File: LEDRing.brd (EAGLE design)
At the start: 52.5 x 52.4 mm, 35 parts, among them U1 ATMEGA328P-AU, U2 MCP73831, U3 MIC5219 3.3V, U4 MMA8452Q, Y1 16MHZ

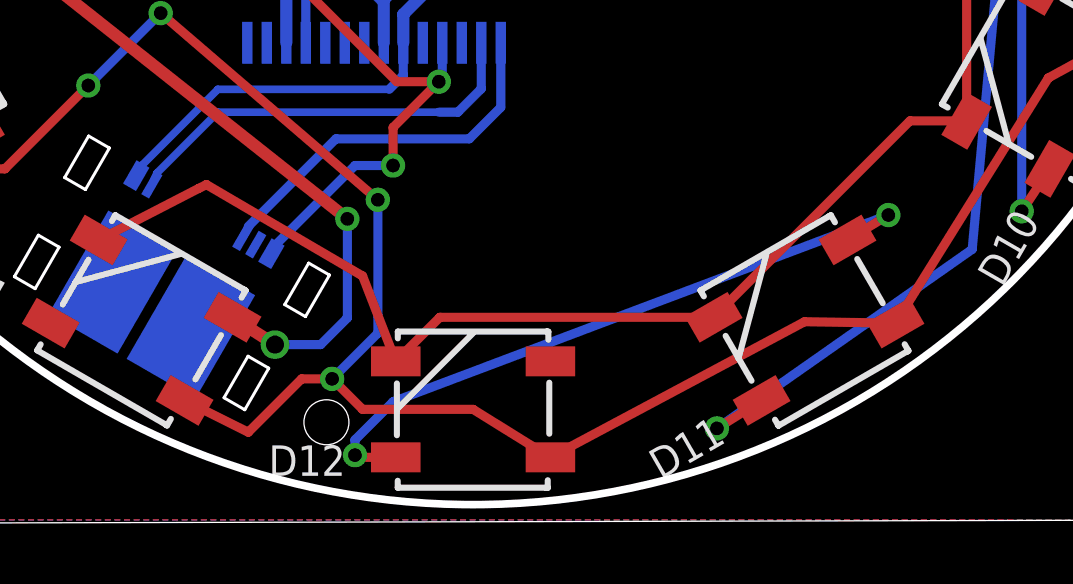
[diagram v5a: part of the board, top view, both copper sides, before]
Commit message: Removed most USB footprint errors
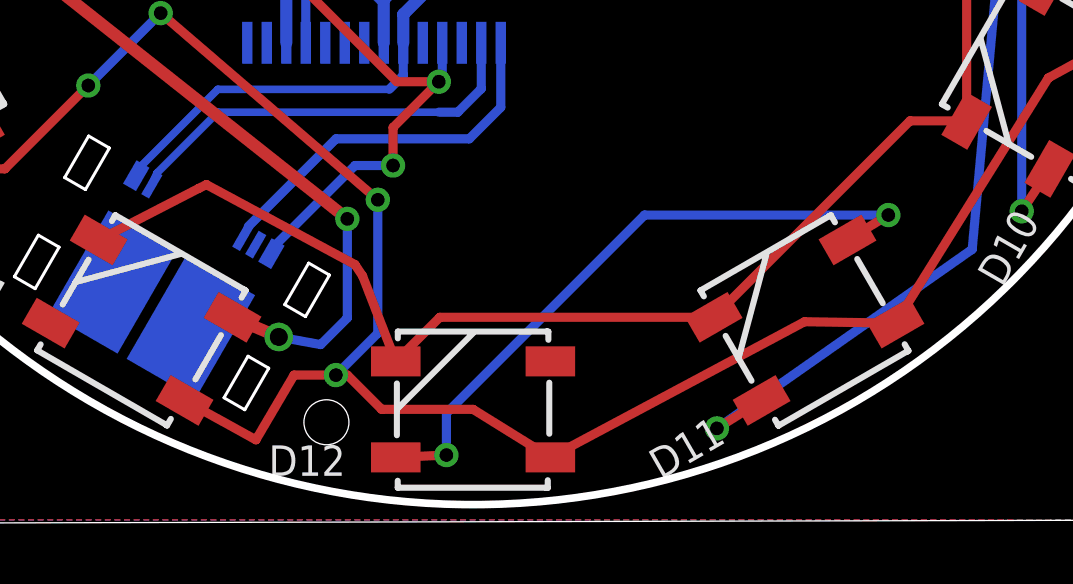
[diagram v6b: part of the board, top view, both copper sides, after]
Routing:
- net N$24: track 22.9 -> 22.1 mm
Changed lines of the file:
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@@
 <wire x1="23.495" y1="11.938" x2="23.495" y2="13.208" width="0.3048" layer="1"/>
 <wire x1="23.495" y1="13.208" x2="25.019" y2="14.732" width="0.3048" layer="1"/>
-<wire x1="29.171" y1="37.592" x2="31.50611875" y2="39.543221875" width="0" layer="19" extent="1-1"/>
-<wire x1="28.956" y1="37.084" x2="29.171" y2="37.592" width="0" layer="19" extent="1-16"/>
-<wire x1="24.887" y1="26.535" x2="26.162" y2="27.31" width="0" layer="19" extent="1-1"/>
-<wire x1="35.5901" y1="27.051" x2="33.655" y2="27.012" width="0" layer="19" extent="1-16"/>
-<wire x1="18.2372" y1="36.2712" x2="26.4668" y2="37.0586" width="0" layer="19" extent="16-16"/>
-<wire x1="18.2372" y1="37.8714" x2="18.2372" y2="36.2712" width="0" layer="19" extent="16-16"/>
-<wire x1="15.748" y1="39.878" x2="18.2372" y2="37.8714" width="0" layer="19" extent="16-16"/>
 </signal>
 <signal name="N$1">
@@
 <wire x1="44.45" y1="31.877" x2="48.26" y2="31.877" width="0.3048" layer="16"/>
 <wire x1="48.26" y1="31.877" x2="49.911" y2="30.226" width="0.3048" layer="16"/>
-<wire x1="26.162" y1="3.81" x2="22.479" y2="3.81" width="0.3048" layer="1"/>
-<wire x1="22.479" y1="3.81" x2="21.463" y2="4.826" width="0.3048" layer="1"/>
-<wire x1="20.447" y1="4.826" x2="18.669" y2="3.048" width="0.3048" layer="1"/>
-<wire x1="18.669" y1="3.048" x2="16.544746875" y2="4.10765625" width="0.3048" layer="1"/>
+<wire x1="20.193" y1="4.953" x2="18.923" y2="2.794" width="0.3048" layer="1"/>
+<wire x1="18.923" y1="2.794" x2="16.544746875" y2="4.10765625" width="0.3048" layer="1"/>
 <wire x1="6.93865625" y1="11.82725" x2="10.55725" y2="11.82725" width="0.3048" layer="1"/>
 <wire x1="10.55725" y1="11.82725" x2="13.335" y2="14.605" width="0.3048" layer="1"/>
@@
 <via x="15.748" y="17.018" extent="1-16" drill="0.4572" diameter="0.254" shape="octagon"/>
 <wire x1="15.748" y1="17.018" x2="22.987" y2="10.795" width="0.3048" layer="1"/>
-<wire x1="20.447" y1="4.826" x2="21.463" y2="4.826" width="0.3048" layer="1"/>
-<via x="21.463" y="4.826" extent="1-16" drill="0.4572" diameter="0.254" shape="octagon"/>
+<wire x1="20.193" y1="4.953" x2="21.59" y2="4.953" width="0.3048" layer="1"/>
+<via x="21.59" y="4.953" extent="1-16" drill="0.4572" diameter="0.254" shape="octagon"/>
 <via x="22.987" y="10.795" extent="1-16" drill="0.4572" diameter="0.254" shape="octagon"/>
 <wire x1="22.987" y1="10.795" x2="22.987" y2="6.35" width="0.3048" layer="16"/>
-<wire x1="22.987" y1="6.35" x2="21.463" y2="4.826" width="0.3048" layer="16"/>
+<wire x1="22.987" y1="6.35" x2="21.59" y2="4.953" width="0.3048" layer="16"/>
+<wire x1="21.59" y1="4.953" x2="21.971" y2="4.953" width="0.3048" layer="1"/>
+<wire x1="21.971" y1="4.953" x2="23.114" y2="3.81" width="0.3048" layer="1"/>
+<wire x1="23.114" y1="3.81" x2="26.162" y2="3.81" width="0.3048" layer="1"/>
 </signal>
 <signal name="V3_3">
@@
 <wire x1="7.132940625" y1="27.016059375" x2="5.664" y2="28.485" width="0.3048" layer="1"/>
 <wire x1="23.585" y1="5.41" x2="22.479" y2="8.255" width="0.3048" layer="1"/>
-<wire x1="22.479" y1="8.255" x2="17.272" y2="11.303" width="0.3048" layer="1"/>
 <wire x1="17.272" y1="11.303" x2="17.018" y2="11.176" width="0.3048" layer="1"/>
 <wire x1="17.018" y1="11.176" x2="13.68125" y2="9.455940625" width="0.3048" layer="1"/>
@@
 <wire x1="33.782" y1="43.307" x2="31.838" y2="43.307" width="0.4064" layer="1"/>
 <wire x1="31.838" y1="43.307" x2="28.739" y2="46.406" width="0.4064" layer="1"/>
+<wire x1="22.479" y1="8.255" x2="22.225" y2="8.636" width="0.3048" layer="1"/>
+<wire x1="22.225" y1="8.636" x2="17.272" y2="11.303" width="0.3048" layer="1"/>
 </signal>
 <signal name="N$10">
@@
 <wire x1="4.36165625" y1="16.290746875" x2="3.556" y2="17.653" width="0.3048" layer="1"/>
 <via x="3.556" y="17.653" extent="1-16" drill="0.4572" diameter="0.254" shape="octagon"/>
-<wire x1="18.144746875" y1="6.878940625" x2="19.558" y2="5.969" width="0.4064" layer="1"/>
-<via x="19.558" y="5.969" extent="1-16" drill="0.6" shape="octagon"/>
+<wire x1="18.144746875" y1="6.878940625" x2="19.685" y2="6.223" width="0.4064" layer="1"/>
+<via x="19.685" y="6.223" extent="1-16" drill="0.6" shape="octagon"/>
 <via x="21.971" y="10.16" extent="1-16" drill="0.4572" diameter="0.254" shape="octagon"/>
 <wire x1="21.971" y1="10.16" x2="8.509" y2="20.828" width="0.4064" layer="1"/>
@@
 <wire x1="21.971" y1="10.16" x2="21.971" y2="6.858" width="0.3048" layer="16"/>
 <wire x1="21.971" y1="6.858" x2="21.082" y2="5.969" width="0.3048" layer="16"/>
-<wire x1="21.082" y1="5.969" x2="19.558" y2="5.969" width="0.3048" layer="16"/>
+<wire x1="21.082" y1="5.969" x2="19.685" y2="6.223" width="0.3048" layer="16"/>
 </signal>
 <signal name="N$16">
@@
 <via x="40.005" y="10.287" extent="1-16" drill="0.4572" diameter="0.254" shape="octagon"/>
 <wire x1="38.642746875" y1="9.455940625" x2="40.005" y2="10.287" width="0.3048" layer="1"/>
-<wire x1="23.585" y1="2.21" x2="22.301" y2="2.21" width="0.3048" layer="1"/>
-<wire x1="22.301" y1="2.21" x2="22.225" y2="2.286" width="0.3048" layer="1"/>
-<via x="22.225" y="2.286" extent="1-16" drill="0.4572" diameter="0.254" shape="octagon"/>
-<wire x1="22.225" y1="2.286" x2="22.225" y2="2.794" width="0.3048" layer="16"/>
-<wire x1="22.225" y1="2.794" x2="23.495" y2="4.064" width="0.3048" layer="16"/>
-<wire x1="23.495" y1="4.064" x2="40.005" y2="10.287" width="0.3048" layer="16"/>
+<via x="25.273" y="2.286" extent="1-16" drill="0.4572" diameter="0.254" shape="octagon"/>
+<wire x1="23.585" y1="2.21" x2="25.273" y2="2.286" width="0.3048" layer="1"/>
+<wire x1="40.005" y1="10.287" x2="31.877" y2="10.287" width="0.3048" layer="16"/>
+<wire x1="31.877" y1="10.287" x2="25.273" y2="3.683" width="0.3048" layer="16"/>
+<wire x1="25.273" y1="3.683" x2="25.273" y2="2.286" width="0.3048" layer="16"/>
 </signal>
 <signal name="N$14">

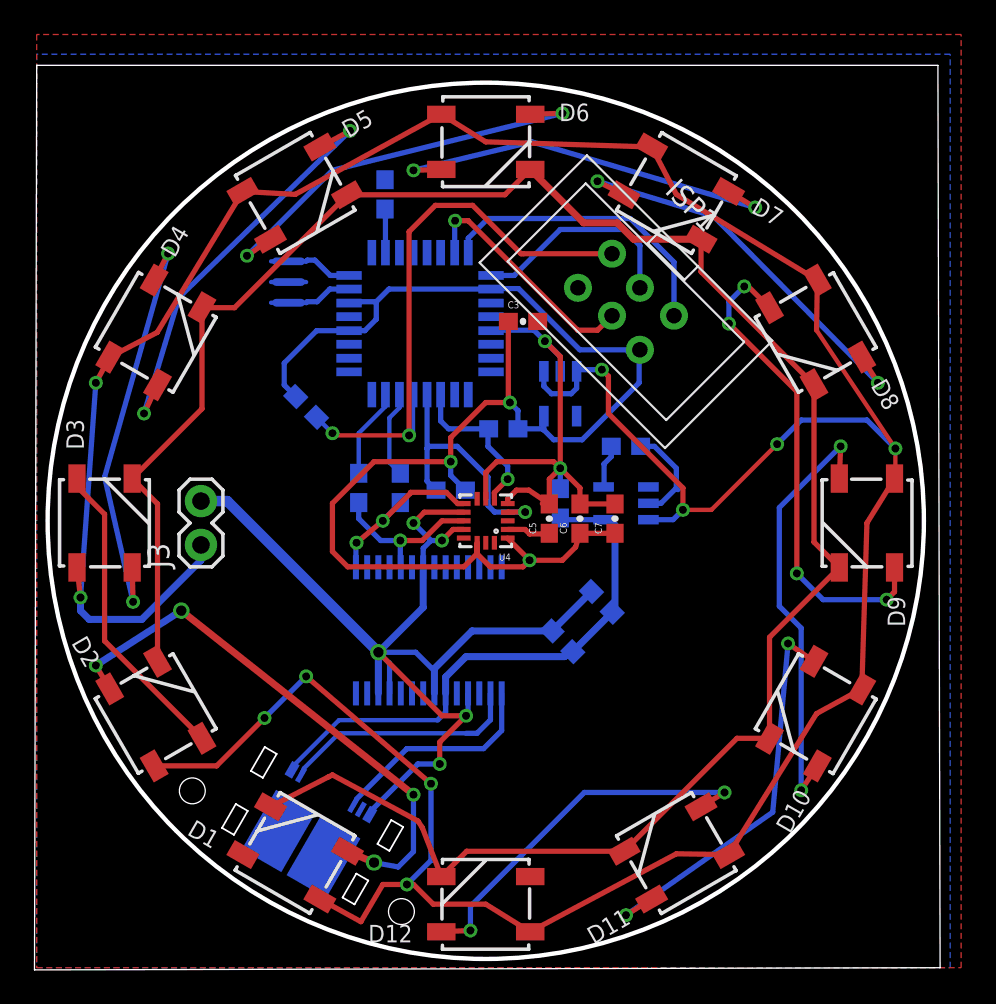
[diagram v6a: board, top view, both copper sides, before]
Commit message: Moved LEDs so USB fits
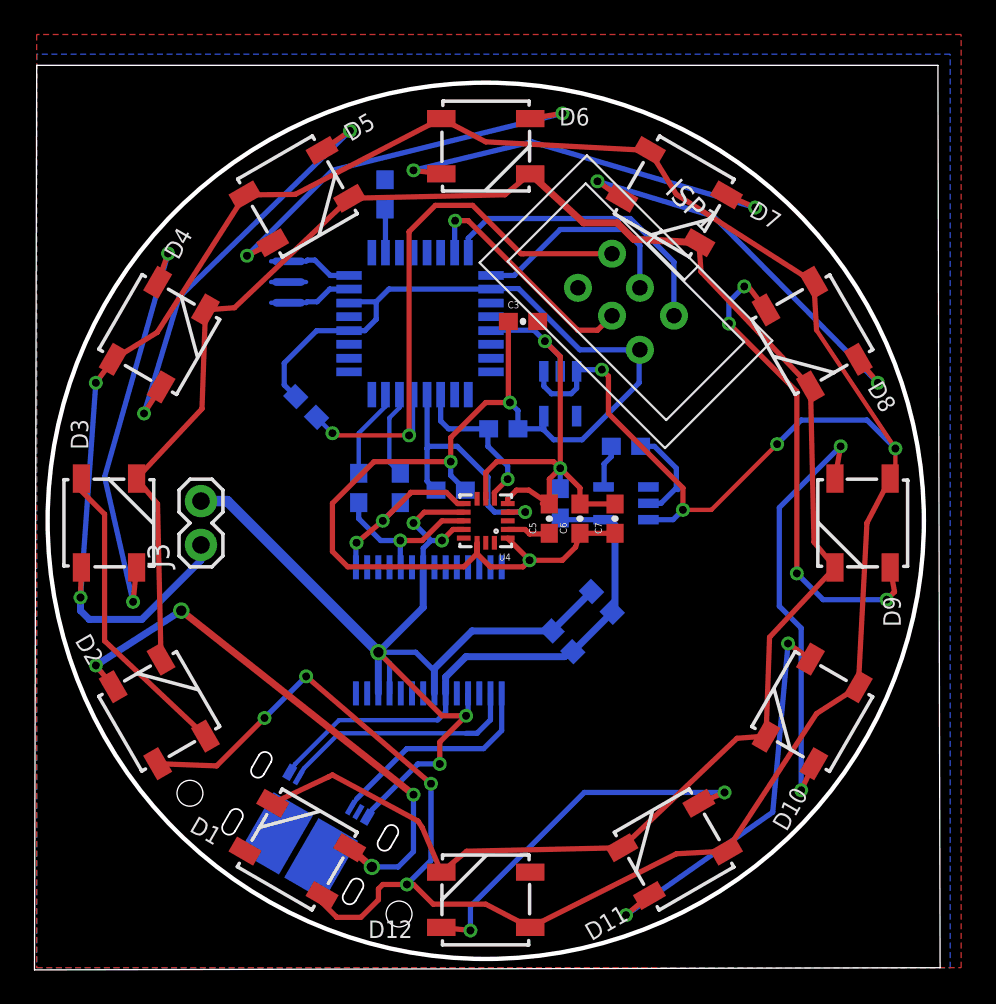
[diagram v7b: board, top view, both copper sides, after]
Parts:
- moved D12 0.25 mm to (26.2, 4.06)
- moved D3 0.25 mm to (4.32, 25.9)
- moved D6 0.25 mm to (26.2, 47.8)
- moved D9 0.25 mm to (48.0, 25.9)
- moved D8 0.24 mm to (45.1, 36.8)
- moved D10 0.24 mm to (45.1, 15.0)
- moved D4 0.24 mm to (7.24, 36.8)
- moved D1 0.24 mm to (15.2, 6.99)
- moved D2 0.24 mm to (7.24, 15.0)
- moved D11 0.24 mm to (37.1, 6.99)
- moved D5 0.24 mm to (15.2, 44.8)
- moved D7 0.24 mm to (37.1, 44.8)
- moved U$2 0.20 mm to (14.2, 5.18)
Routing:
- net VSS: track 126.2 -> 122.9 mm
- net VBATT: track 202.4 -> 200.7 mm

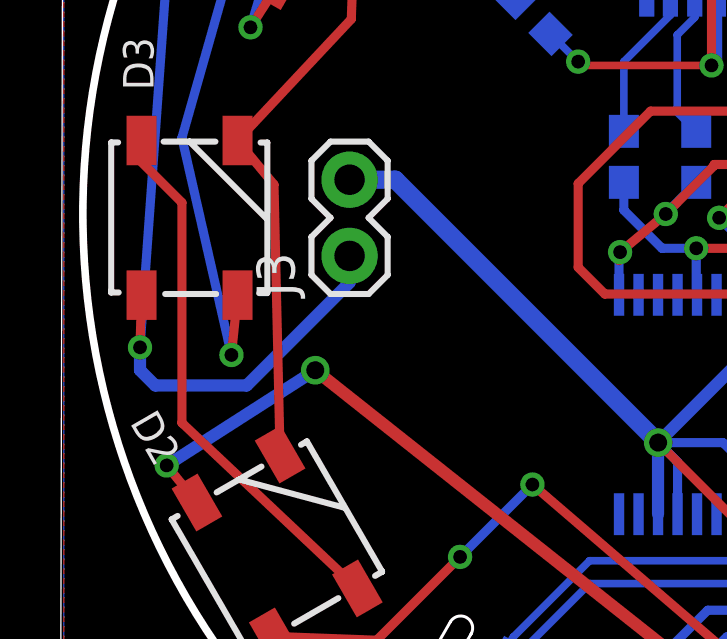
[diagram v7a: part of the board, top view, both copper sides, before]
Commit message: Started tieing LED VSS to GND
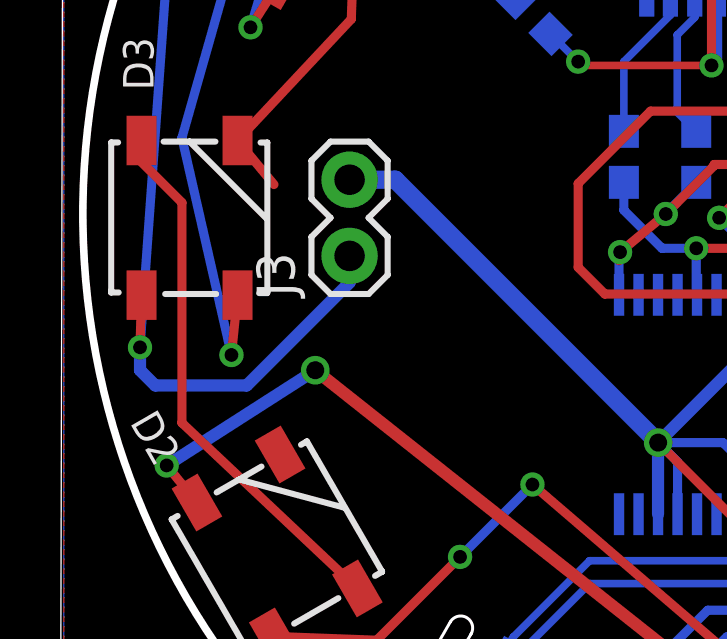
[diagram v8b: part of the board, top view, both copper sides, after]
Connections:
- net GND: now also D2.3
- net VSS: no longer D2.3
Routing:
- net VSS: track 122.9 -> 113.9 mm
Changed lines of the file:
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@@
 <wire x1="23.495" y1="11.938" x2="23.495" y2="13.208" width="0.3048" layer="1"/>
 <wire x1="23.495" y1="13.208" x2="25.019" y2="14.732" width="0.3048" layer="1"/>
+<contactref element="D2" pad="3"/>
 </signal>
 <signal name="N$1">
@@
 <signal name="VSS">
 <contactref element="D1" pad="3"/>
-<contactref element="D2" pad="3"/>
 <contactref element="D3" pad="3"/>
 <contactref element="D4" pad="3"/>
@@
 <wire x1="34.05225" y1="7.082140625" x2="25.053940625" y2="6.878940625" width="0.3048" layer="1"/>
 <wire x1="25.053940625" y1="6.878940625" x2="23.585" y2="5.664" width="0.3048" layer="1"/>
-<wire x1="7.336140625" y1="18.017746875" x2="7.132940625" y2="27.016059375" width="0.3048" layer="1"/>
 <wire x1="7.132940625" y1="27.016059375" x2="5.918" y2="28.485" width="0.3048" layer="1"/>
 <wire x1="23.585" y1="5.664" x2="22.479" y2="8.255" width="0.3048" layer="1"/>
